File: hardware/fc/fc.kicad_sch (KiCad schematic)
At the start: 0 parts

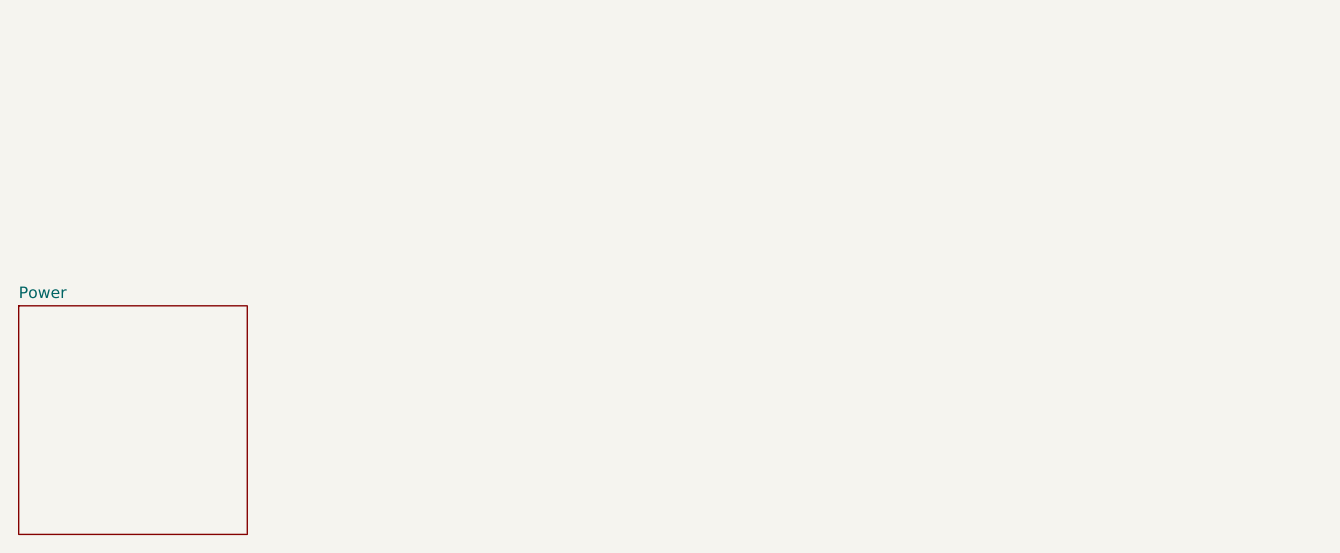
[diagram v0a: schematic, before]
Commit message: fc: add peripherals and sensors
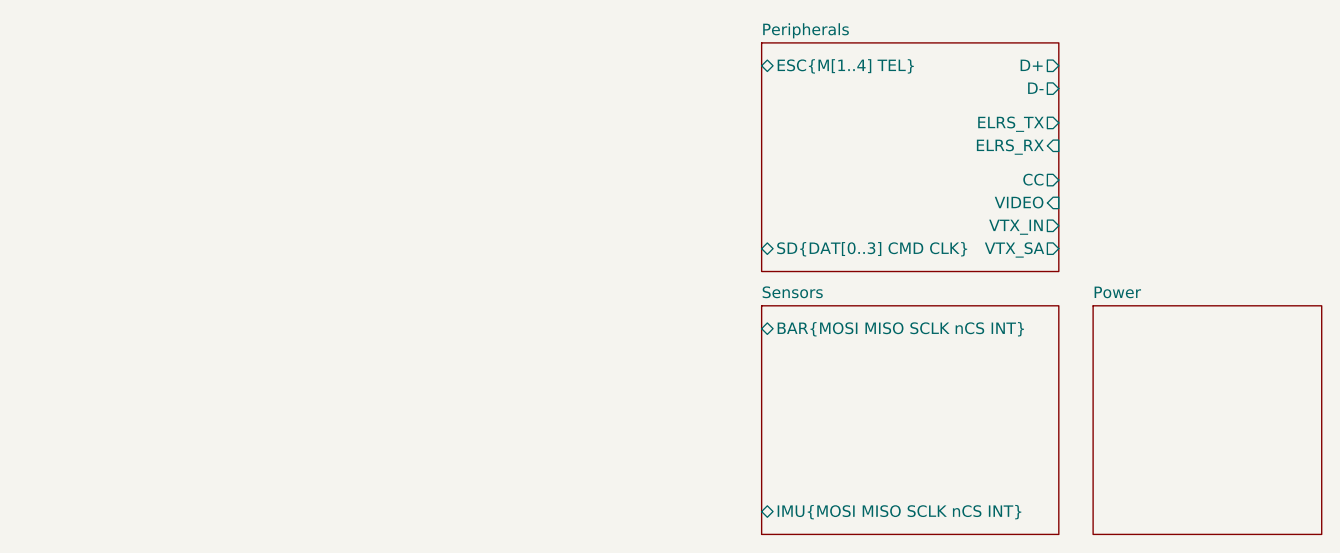
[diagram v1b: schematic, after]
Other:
- added sheet Peripherals (peripherals.kicad_sch)
- added sheet Sensors (sensors.kicad_sch)
- title: (none) -> RP2354B; BMP580; ICM-42688-P Flight Controller
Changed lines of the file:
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@@
 	(generator_version "10.0")
 	(paper "A4")
+	(title_block
+		(title "RP2354B; BMP580; ICM-42688-P Flight Controller")
+		(date "2026-09-17")
+		(rev "1")
+	)
 	(sheet
-		(at 106.68 104.14)
+		(at 189.23 74.93)
+		(size 33.02 25.4)
+		(exclude_from_sim no)
+		(in_bom yes)
+		(on_board yes)
+		(dnp no)
+		(fields_autoplaced yes)
+		(stroke
+			(width 0.1524)
+			(type solid)
+		)
+		(fill
+			(color 0 0 0 0)
+		)
+		(property "Sheetname" "Peripherals"
+			(at 189.23 74.2184 0)
+			(show_name no)
+			(do_not_autoplace no)
+			(effects
+				(font
+					(size 1.27 1.27)
+				)
+				(justify left bottom)
+			)
+		)
+		(property "Sheetfile" "peripherals.kicad_sch"
+			(at 189.23 100.9146 0)
+			(hide yes)
+			(show_name no)
+			(do_not_autoplace no)
+			(effects
+				(font
+					(size 1.27 1.27)
+				)
+				(justify left top)
+			)
+		)
+		(pin "ELRS_RX" input
+			(at 222.25 86.36 0)
+			(effects
+				(font
+					(size 1.27 1.27)
+				)
+				(justify right)
+			)
+		)
+		(pin "ESC{M[1..4] TEL}" bidirectional
+			(at 189.23 77.47 180)
+			(effects
+				(font
+					(size 1.27 1.27)
+				)
+				(justify left)
+			)
+		)
+		(pin "SD{DAT[0..3] CMD CLK}" bidirectional
+			(at 189.23 97.79 180)
+			(effects
+				(font
+					(size 1.27 1.27)
+				)
+				(justify left)
+			)
+		)
+		(pin "VIDEO" input
+			(at 222.25 92.71 0)
+			(effects
+				(font
+					(size 1.27 1.27)
+				)
+				(justify right)
+			)
+		)
+		(pin "CC" output
+			(at 222.25 90.17 0)
+			(effects
+				(font
+					(size 1.27 1.27)
+				)
+				(justify right)
+			)
+		)
+		(pin "D+" output
+			(at 222.25 77.47 0)
+			(effects
+				(font
+					(size 1.27 1.27)
+				)
+				(justify right)
+			)
+		)
+		(pin "D-" output
+			(at 222.25 80.01 0)
+			(effects
+				(font
+					(size 1.27 1.27)
+				)
+				(justify right)
+			)
+		)
+		(pin "ELRS_TX" output
+			(at 222.25 83.82 0)
+			(effects
+				(font
+					(size 1.27 1.27)
+				)
+				(justify right)
+			)
+		)
+		(pin "VTX_IN" output
+			(at 222.25 95.25 0)
+			(effects
+				(font
+					(size 1.27 1.27)
+				)
+				(justify right)
+			)
+		)
+		(pin "VTX_SA" output
+			(at 222.25 97.79 0)
+			(effects
+				(font
+					(size 1.27 1.27)
+				)
+				(justify right)
+			)
+		)
+		(instances
+			(project "fc"
+				(path "/6eb6d89e-9d71-4347-9ba3-a394c00e5720"
+					(page "3")
+				)
+			)
+		)
+	)
+	(sheet
+		(at 189.23 104.14)
+		(size 33.02 25.4)
+		(exclude_from_sim no)
+		(in_bom yes)
+		(on_board yes)
+		(dnp no)
+		(fields_autoplaced yes)
+		(stroke
+			(width 0.1524)
+			(type solid)
+		)
+		(fill
+			(color 0 0 0 0)
+		)
+		(property "Sheetname" "Sensors"
+			(at 189.23 103.4284 0)
+			(show_name no)
+			(do_not_autoplace no)
+			(effects
+				(font
+					(size 1.27 1.27)
+				)
+				(justify left bottom)
+			)
+		)
+		(property "Sheetfile" "sensors.kicad_sch"
+			(at 189.23 130.1246 0)
+			(hide yes)
+			(show_name no)
+			(do_not_autoplace no)
+			(effects
+				(font
+					(size 1.27 1.27)
+				)
+				(justify left top)
+			)
+		)
+		(pin "BAR{MOSI MISO SCLK nCS INT}" bidirectional
+			(at 189.23 106.68 180)
+			(effects
+				(font
+					(size 1.27 1.27)
+				)
+				(justify left)
+			)
+		)
+		(pin "IMU{MOSI MISO SCLK nCS INT}" bidirectional
+			(at 189.23 127 180)
+			(effects
+				(font
+					(size 1.27 1.27)
+				)
+				(justify left)
+			)
+		)
+		(instances
+			(project "fc"
+				(path "/6eb6d89e-9d71-4347-9ba3-a394c00e5720"
+					(page "4")
+				)
+			)
+		)
+	)
+	(sheet
+		(at 226.06 104.14)
 		(size 25.4 25.4)
 		(exclude_from_sim no)
@@
 		)
 		(property "Sheetname" "Power"
-			(at 106.68 103.4284 0)
+			(at 226.06 103.4284 0)
 			(show_name no)
 			(do_not_autoplace no)
@@
 		)
 		(property "Sheetfile" "power.kicad_sch"
-			(at 106.68 130.1246 0)
+			(at 226.06 130.1246 0)
 			(hide yes)
 			(show_name no)

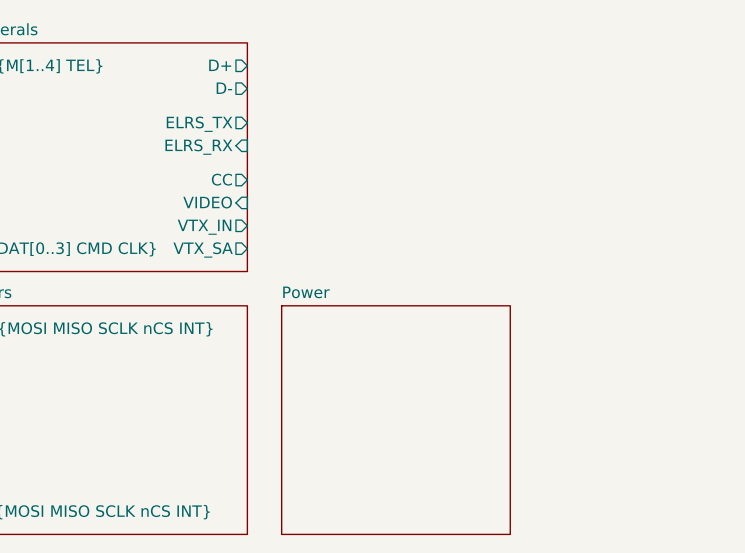
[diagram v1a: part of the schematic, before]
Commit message: fc: add 5V mux and OSD
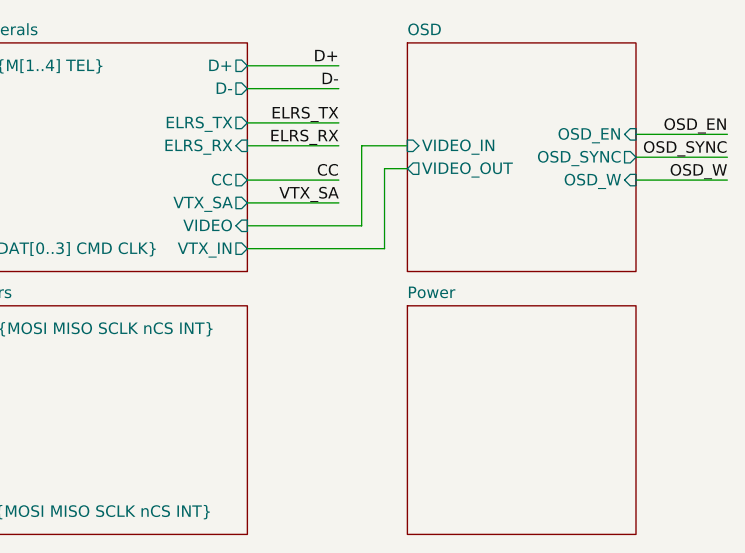
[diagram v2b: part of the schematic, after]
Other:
- added sheet OSD (osd.kicad_sch)
- title: RP2354B; BMP580; ICM-42688-P Flight Controller -> RP2354B; BMP580; ICM-40609-D Flight Controller

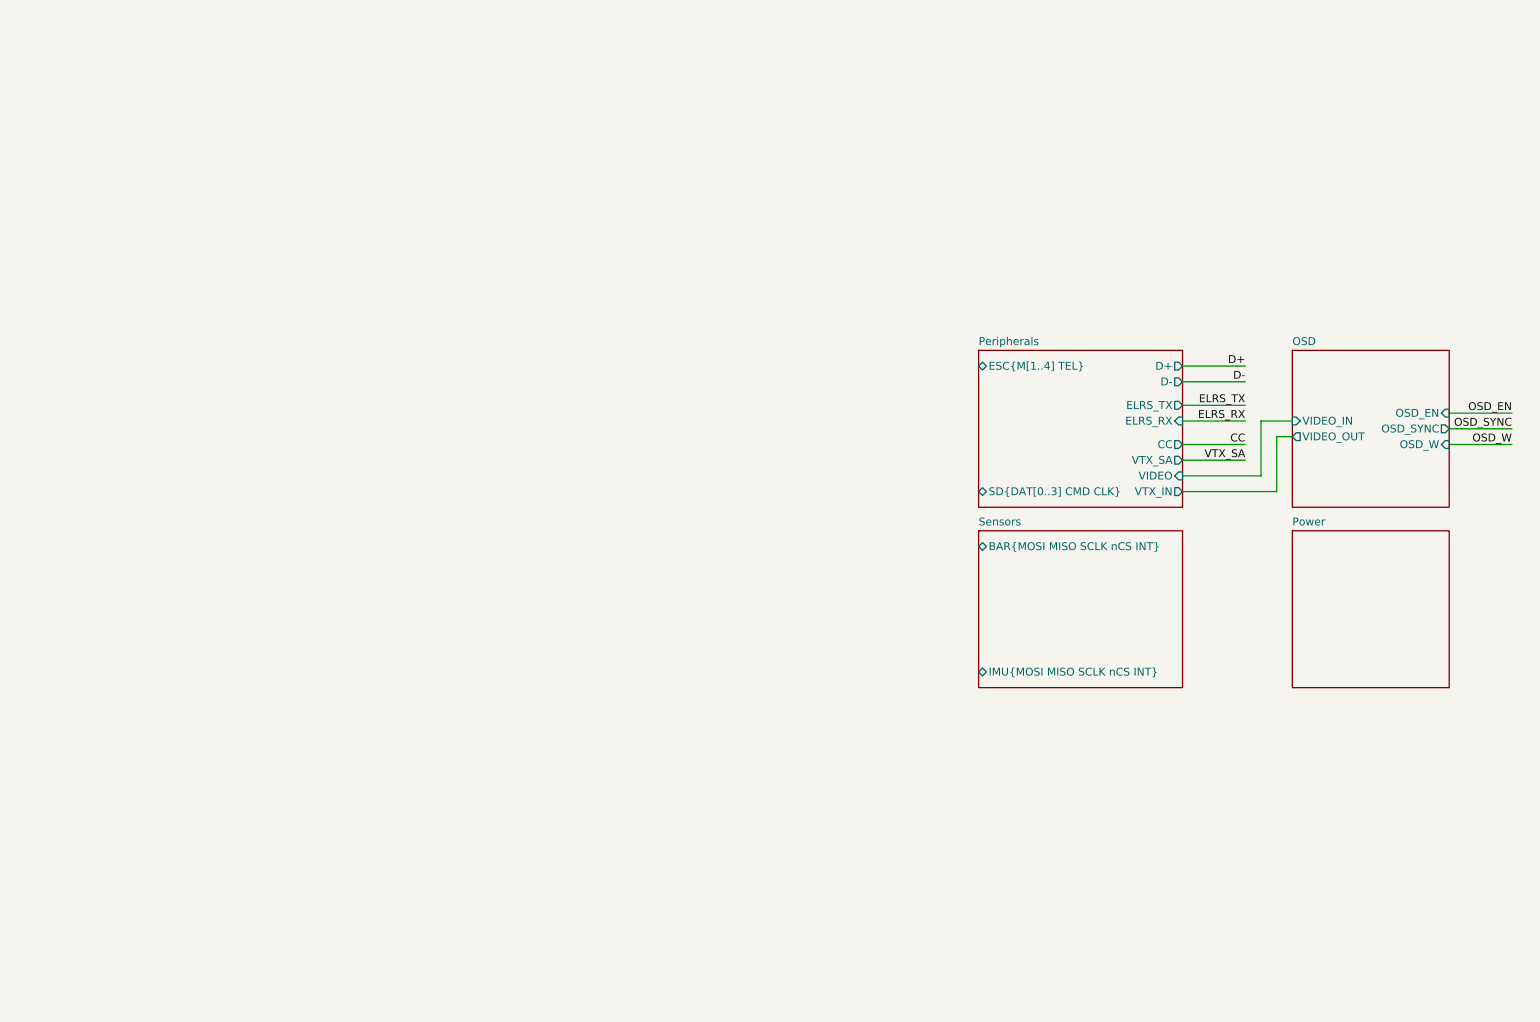
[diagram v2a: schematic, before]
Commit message: fc: update formatting; route RP2354 passives
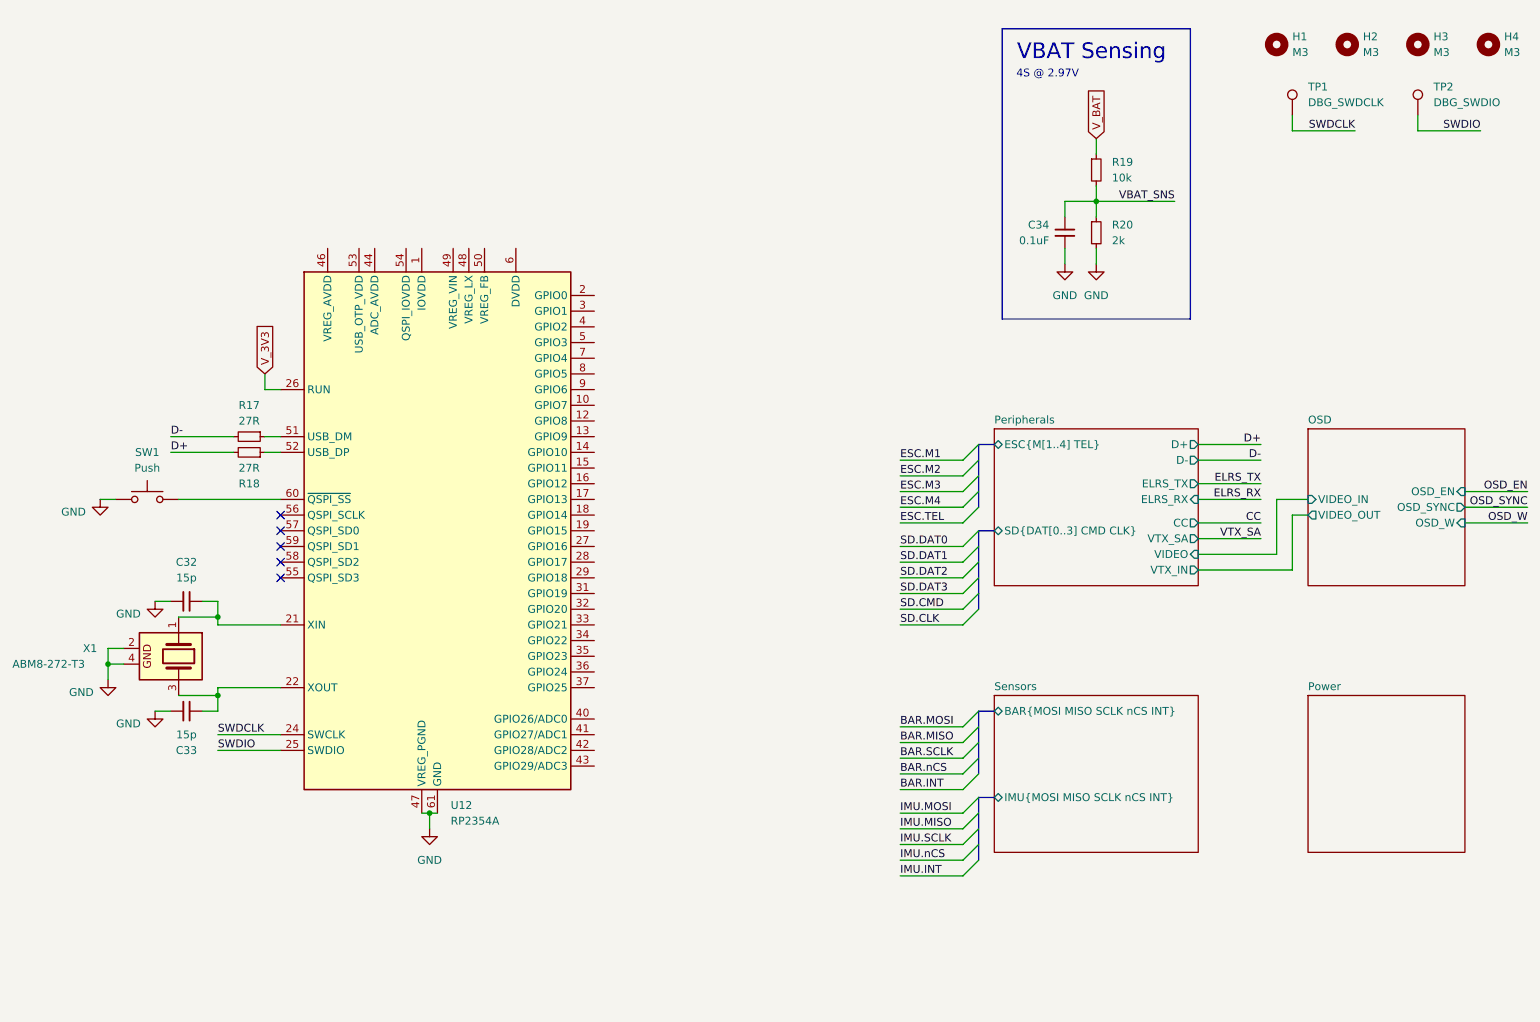
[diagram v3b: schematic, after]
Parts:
- added C32, C33: 15p, PCM_Crystal_AKL:Crystal_SMD_3225-4Pin_3.2x2.5mm, symbol Device:C_Small
- added C34: 0.1uF, PCM_Crystal_AKL:Crystal_SMD_3225-4Pin_3.2x2.5mm, symbol Device:C_Small
- added H1, H2, H3, H4: M3, symbol Mechanical:MountingHole
- added R17, R18: 27R, symbol Device:R_Small
- added R19: 10k, symbol Device:R_Small
- added R20: 2k, symbol Device:R_Small
- added SW1: Push, symbol Switch:SW_Push
- added TP1: DBG_SWDCLK, symbol Connector:TestPoint
- added TP2: DBG_SWDIO, symbol Connector:TestPoint
- added U12: RP2354A, Package_DFN_QFN:QFN-60-1EP_7x7mm_P0.4mm_EP3.4x3.4mm, symbol MCU_RaspberryPi:RP2354A
- added X1: ABM8-272-T3, PCM_Crystal_AKL:Crystal_SMD_3225-4Pin_3.2x2.5mm, symbol PCM_Crystal_AKL:SMD3225-4
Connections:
- net D+: now also R18.2
- net D-: now also R17.2
- new net: U12.1 (IOVDD), U12.11 (IOVDD), U12.20 (IOVDD), U12.30 (IOVDD), U12.38 (IOVDD), U12.45 (IOVDD)
- new net: C32.1, U12.21 (XIN), X1.1
- new net: C33.1, U12.22 (XOUT), X1.3
- new net: U12.23 (DVDD), U12.39 (DVDD), U12.6 (DVDD)
- new net: R17.1, U12.51 (USB_DM)
- new net: R18.1, U12.52 (USB_DP)
- new net: SW1.2, U12.60 (~{QSPI_SS})
- new net GND: C32.2, C33.2, C34.2, R20.2, SW1.1, U12.47 (VREG_PGND), U12.61 (GND), X1.2, X1.4
- new net SWDCLK: TP1.1, U12.24 (SWCLK)
- new net SWDIO: TP2.1, U12.25 (SWDIO)
- new net VBAT_SNS: C34.1, R19.2, R20.1
- new net V_3V3: U12.26 (RUN)
- new net V_BAT: R19.1
- no-connect marks 0 -> 5
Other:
- note added: "4S @ 2.97V"
- note added: "VBAT Sensing"

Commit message: fc: delete barometer; finalise schematic
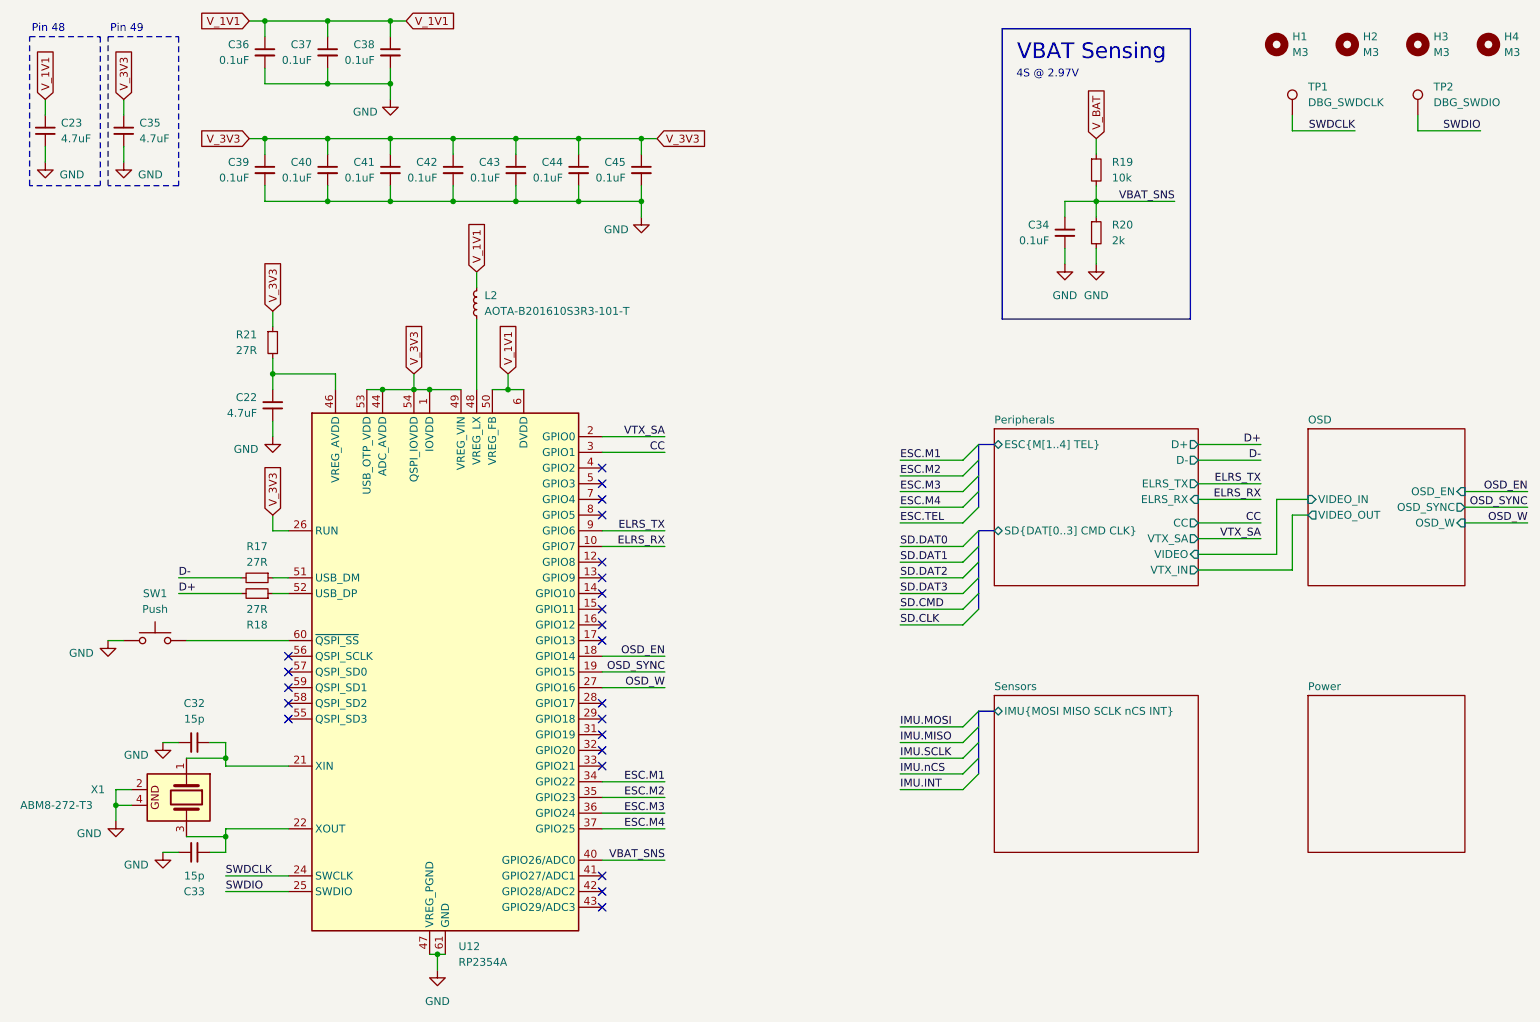
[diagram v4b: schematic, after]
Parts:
- added C22, C23, C35: 4.7uF, symbol Device:C_Small
- added C36, C37, C38, C39, C40, C41, C42, C43, C44, C45: 0.1uF, symbol Device:C_Small
- added L2: AOTA-B201610S3R3-101-T, PCM_Package_SO_AKL:SO-8_3.9x4.9mm_P1.27mm, symbol Device:L_Small
- added R21: 27R, symbol Device:R_Small
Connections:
- net CC: now also U12.3 (GPIO1)
- net ELRS_RX: now also U12.10 (GPIO7)
- net ELRS_TX: now also U12.9 (GPIO6)
- net ESC.M1: now also U12.34 (GPIO22)
- net ESC.M2: now also U12.35 (GPIO23)
- net ESC.M3: now also U12.36 (GPIO24)
- net ESC.M4: now also U12.37 (GPIO25)
- net GND: now also C22.2, C23.2, C35.2, C36.2, C37.2, C38.2, C39.2, C40.2, C41.2, C42.2, C43.2, C44.2, C45.2
- net OSD_EN: now also U12.18 (GPIO14)
- net OSD_SYNC: now also U12.19 (GPIO15)
- net OSD_W: now also U12.27 (GPIO16)
- net VBAT_SNS: now also U12.40 (GPIO26/ADC0)
- net VTX_SA: now also U12.2 (GPIO0)
- net V_3V3: now also U12.1 (IOVDD), U12.11 (IOVDD), U12.20 (IOVDD), U12.30 (IOVDD), U12.38 (IOVDD), U12.44 (ADC_AVDD), U12.45 (IOVDD), U12.49 (VREG_VIN), U12.53 (USB_OTP_VDD), U12.54 (QSPI_IOVDD), C35.1, C39.1, C40.1, C41.1, C42.1, C43.1, C44.1, C45.1, R21.1
- net V_1V1: now reaches U12.23 (DVDD), U12.39 (DVDD), U12.6 (DVDD)
- net V_1V1: now also U12.50 (VREG_FB), C23.1, C36.1, C37.1, C38.1, L2.2
- net at U12.46 (VREG_AVDD): now also C22.1, R21.2
- net at U12.48 (VREG_LX): now also L2.1
- no-connect marks 5 -> 23
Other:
- sheet Sensors ports: added none; removed BAR{MOSI MISO SCLK nCS INT}
- note added: "Pin 48"
- note added: "Pin 49"
- title: RP2354B; BMP580; ICM-40609-D Flight Controller -> RP2354B; ICM-40609-D Flight Controller
- moved on the sheet: C32, C33, R17, R18, SW1, U12, X1
